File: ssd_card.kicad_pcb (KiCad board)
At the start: 2 copper layers, 135.6 x 54 mm, 1 part, among them J1 SmartCard_ISO7816

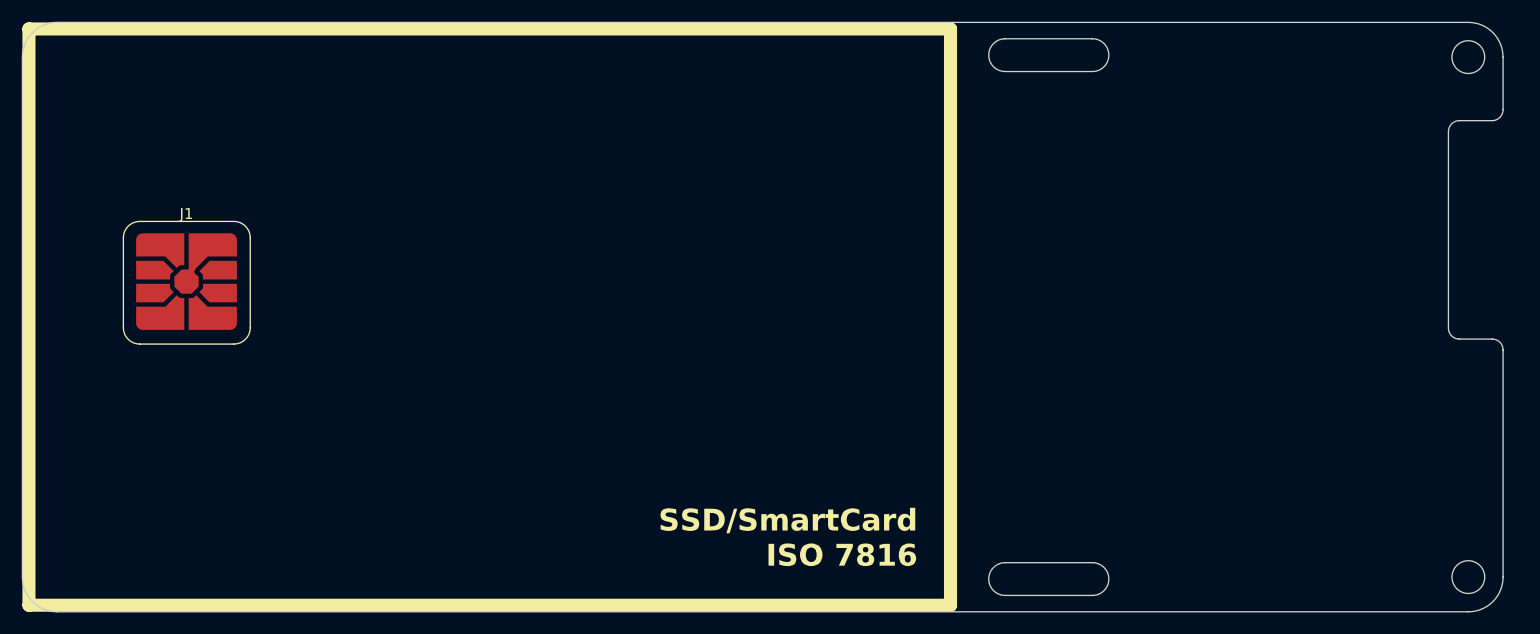
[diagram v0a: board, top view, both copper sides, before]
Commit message: Add HRO USB-C receptacle footprint
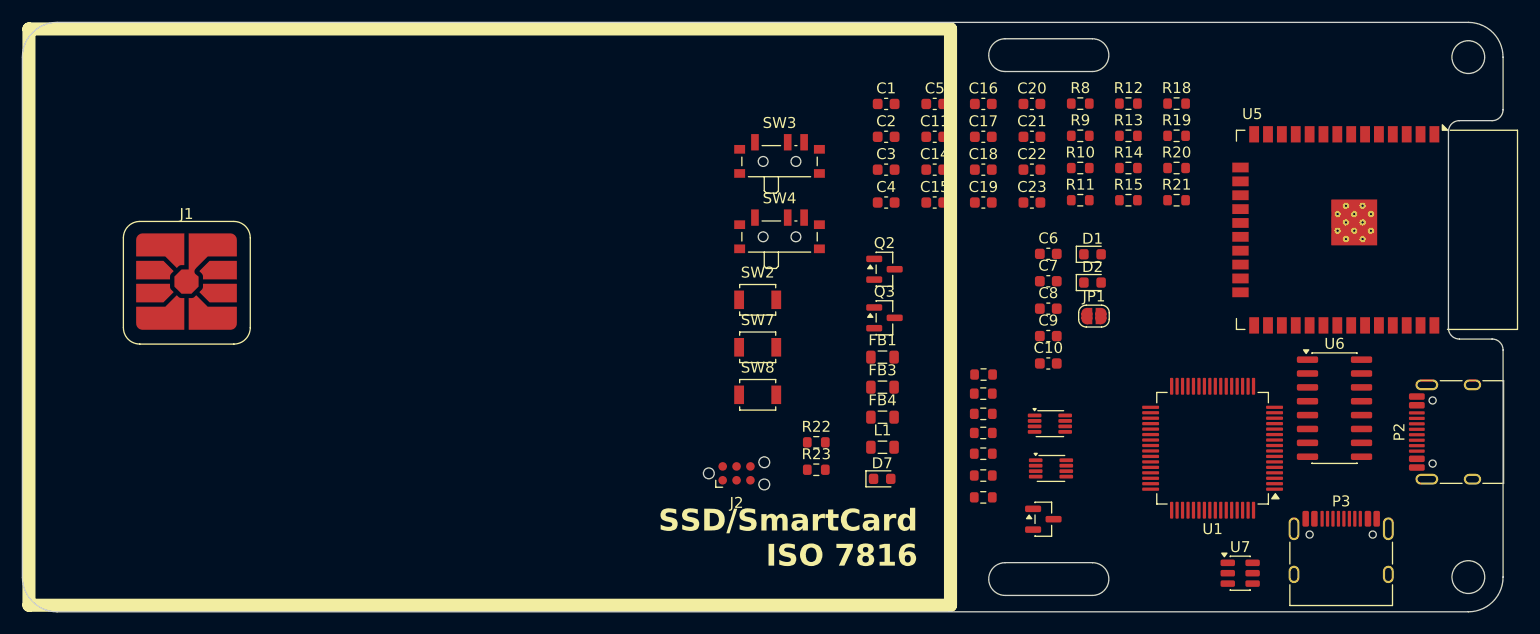
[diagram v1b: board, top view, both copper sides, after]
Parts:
- added C1: 100n, Capacitor_SMD:C_0603_1608Metric, F.Cu at (179.1, 107.5)
- added C10: 2.2uF, Capacitor_SMD:C_0603_1608Metric, F.Cu at (194.0, 131.2)
- added C11: 10uF, Capacitor_SMD:C_0603_1608Metric, F.Cu at (183.6, 110.5)
- added C14: 10uF, Capacitor_SMD:C_0603_1608Metric, F.Cu at (183.6, 113.5)
- added C15: 10uF, Capacitor_SMD:C_0603_1608Metric, F.Cu at (183.6, 116.5)
- added C16: 100n, Capacitor_SMD:C_0603_1608Metric, F.Cu at (188.0, 107.5)
- added C17: 100n, Capacitor_SMD:C_0603_1608Metric, F.Cu at (188.0, 110.5)
- added C18: 100n, Capacitor_SMD:C_0603_1608Metric, F.Cu at (188.0, 113.5)
- added C19: 10uF, Capacitor_SMD:C_0603_1608Metric, F.Cu at (188.0, 116.5)
- added C2: 100n, Capacitor_SMD:C_0603_1608Metric, F.Cu at (179.1, 110.5)
- added C20: 100n, Capacitor_SMD:C_0603_1608Metric, F.Cu at (192.5, 107.5)
- added C21: 100n, Capacitor_SMD:C_0603_1608Metric, F.Cu at (192.5, 110.5)
- added C22: 10uF, Capacitor_SMD:C_0603_1608Metric, F.Cu at (192.5, 113.5)
- added C23: 10uF, Capacitor_SMD:C_0603_1608Metric, F.Cu at (192.5, 116.5)
- added C3: 100n, Capacitor_SMD:C_0603_1608Metric, F.Cu at (179.1, 113.5)
- added C4: 100n, Capacitor_SMD:C_0603_1608Metric, F.Cu at (179.1, 116.5)
- added C5: 100n, Capacitor_SMD:C_0603_1608Metric, F.Cu at (183.6, 107.5)
- added C6: 0.1u, Capacitor_SMD:C_0603_1608Metric, F.Cu at (194.0, 121.2)
- added C7: 20pF, Capacitor_SMD:C_0603_1608Metric, F.Cu at (194.0, 123.7)
- added C8: 20pF, Capacitor_SMD:C_0603_1608Metric, F.Cu at (194.0, 126.2)
- added C9: 2.2uF, Capacitor_SMD:C_0603_1608Metric, F.Cu at (194.0, 128.7)
- added D1: DS, LED_SMD:LED_0603_1608Metric, F.Cu at (198.0, 121.2)
- added D2: DE, LED_SMD:LED_0603_1608Metric, F.Cu at (198.0, 123.8)
- added D7: B, LED_SMD:LED_0603_1608Metric, F.Cu at (178.7, 141.8)
- added FB1: FB, Inductor_SMD:L_0805_2012Metric, F.Cu at (178.8, 130.7)
- added FB3: FB, Inductor_SMD:L_0805_2012Metric, F.Cu at (178.8, 133.4)
- added FB4: FB, Inductor_SMD:L_0805_2012Metric, F.Cu at (178.8, 136.2)
- added J2: SWD_TagConnect_TC2030, Connector:Tag-Connect_TC2030-IDC-NL_2x03_P1.27mm_Vertical, F.Cu at (165.4, 141.3)
- added JP1: SJ_ESP_BOOT, Jumper:SolderJumper-2_P1.3mm_Open_RoundedPad1.0x1.5mm, F.Cu at (198.1, 126.9)
- added L1: 4.7uH, Inductor_SMD:L_0805_2012Metric, F.Cu at (178.8, 138.9)
- added P2: USB_C_Plug_USB2.0, USB_C_HRO:USB_C_Receptacle_HRO_TYPE-C-31-M-12, F.Cu at (231.8, 137.5)
- added P3: USB_C_Plug_USB2.0, USB_C_HRO:USB_C_Receptacle_HRO_TYPE-C-31-M-12, F.Cu at (220.8, 149.5)
- added Q1: 2N7002, Package_TO_SOT_SMD:SOT-23, F.Cu at (193.5, 145.5)
- added Q2: BSS138, Package_TO_SOT_SMD:SOT-23, F.Cu at (178.9, 122.6)
- added Q3: BSS138, Package_TO_SOT_SMD:SOT-23, F.Cu at (178.9, 127.1)
- added R1: 100k, Resistor_SMD:R_0603_1608Metric, F.Cu at (188.0, 132.2)
- added R10: 10K, Resistor_SMD:R_0603_1608Metric, F.Cu at (196.9, 113.3)
- added R11: 10K, Resistor_SMD:R_0603_1608Metric, F.Cu at (196.9, 116.3)
- added R12: 5.1k, Resistor_SMD:R_0603_1608Metric, F.Cu at (201.3, 107.4)
- added R13: 300R, Resistor_SMD:R_0603_1608Metric, F.Cu at (201.3, 110.4)
- added R14: 10K, Resistor_SMD:R_0603_1608Metric, F.Cu at (201.3, 113.3)
- added R15: 5.1k, Resistor_SMD:R_0603_1608Metric, F.Cu at (201.3, 116.3)
- added R18: 10K, Resistor_SMD:R_0603_1608Metric, F.Cu at (205.7, 107.4)
- added R19: 10K, Resistor_SMD:R_0603_1608Metric, F.Cu at (205.7, 110.4)
- added R2: 100k, Resistor_SMD:R_0603_1608Metric, F.Cu at (188.0, 134.0)
- added R20: 1k, Resistor_SMD:R_0603_1608Metric, F.Cu at (205.7, 113.3)
- added R21: 1k, Resistor_SMD:R_0603_1608Metric, F.Cu at (205.7, 116.3)
- added R22: 100K, Resistor_SMD:R_0603_1608Metric, F.Cu at (172.7, 138.5)
- added R23: 100K, Resistor_SMD:R_0603_1608Metric, F.Cu at (172.7, 141.0)
- added R3: 220, Resistor_SMD:R_0603_1608Metric, F.Cu at (188.0, 135.8)
- added R4: 220, Resistor_SMD:R_0603_1608Metric, F.Cu at (188.0, 137.6)
- added R5: 100R, Resistor_SMD:R_0603_1608Metric, F.Cu at (188.0, 139.5)
- added R6: 220, Resistor_SMD:R_0603_1608Metric, F.Cu at (188.0, 143.5)
- added R7: 100k, Resistor_SMD:R_0603_1608Metric, F.Cu at (188.0, 141.5)
- added R8: 10K, Resistor_SMD:R_0603_1608Metric, F.Cu at (196.9, 107.4)
- added R9: 300R, Resistor_SMD:R_0603_1608Metric, F.Cu at (196.9, 110.4)
- added SW2: STM_NRST, Button_Switch_SMD:SW_SPST_B3U-1000P, F.Cu at (167.3, 125.4)
- added SW3: STM_BOOT0_SW, Button_Switch_SMD:SW_SPDT_PCM12, F.Cu at (169.3, 112.4)
- added SW4: ESP32_BOOT_SW, Button_Switch_SMD:SW_SPDT_PCM12, F.Cu at (169.3, 119.3)
- added SW7: STM_SB1, Button_Switch_SMD:SW_SPST_B3U-1000P, F.Cu at (167.3, 129.8)
- added SW8: STM_SB2, Button_Switch_SMD:SW_SPST_B3U-1000P, F.Cu at (167.3, 134.1)
- added U1: STM32F405RGTx, Package_QFP:LQFP-64_10x10mm_P0.5mm, F.Cu at (209.0, 139.0)
- added U2: SN74LVC2T45DCUR, Package_SO:VSSOP-8_2.3x2mm_P0.5mm, F.Cu at (194.1, 136.8)
- added U3: SN74LVC2T45DCUR, Package_SO:VSSOP-8_2.3x2mm_P0.5mm, F.Cu at (194.2, 140.8)
- added U5: ESP32-WROOM-32, RF_Module:ESP32-WROOM-32, F.Cu at (221.1, 119.0)
- added U6: CH340C, Package_SO:SOIC-16_3.9x9.9mm_P1.27mm, F.Cu at (220.2, 135.3)
- added U7: AP63203WU, Package_TO_SOT_SMD:TSOT-23-6, F.Cu at (211.5, 150.4)
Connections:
- J1 pad 1: unconnected-(J1-VCC-Pad1) -> /SC_VCC
- J1 pad 2: unconnected-(J1-RST-Pad2) -> /SC_RST
- J1 pad 3: unconnected-(J1-CLK-Pad3) -> /SC_CLK
- J1 pad 4: unconnected-(J1-AUX1-Pad4) -> /SC_AUX1
- J1 pad 5: unconnected-(J1-GND-Pad5) -> GND
- J1 pad 6: unconnected-(J1-VPP/NC-Pad6) -> /SC_VPP
- J1 pad 7: unconnected-(J1-I/O-Pad7) -> /SC_IO
- J1 pad 8: unconnected-(J1-AUX2-Pad8) -> /SC_AUX2
